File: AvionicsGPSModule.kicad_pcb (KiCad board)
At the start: 4 copper layers, 60 x 56.1 mm, 34 parts, among them P1 MC311D, Q1 AO3400A, U1 RP2040, U2 AP2112K-3.3, U3 L80-R, U4 W25Q128JVS, X1 ABM8-272-T3

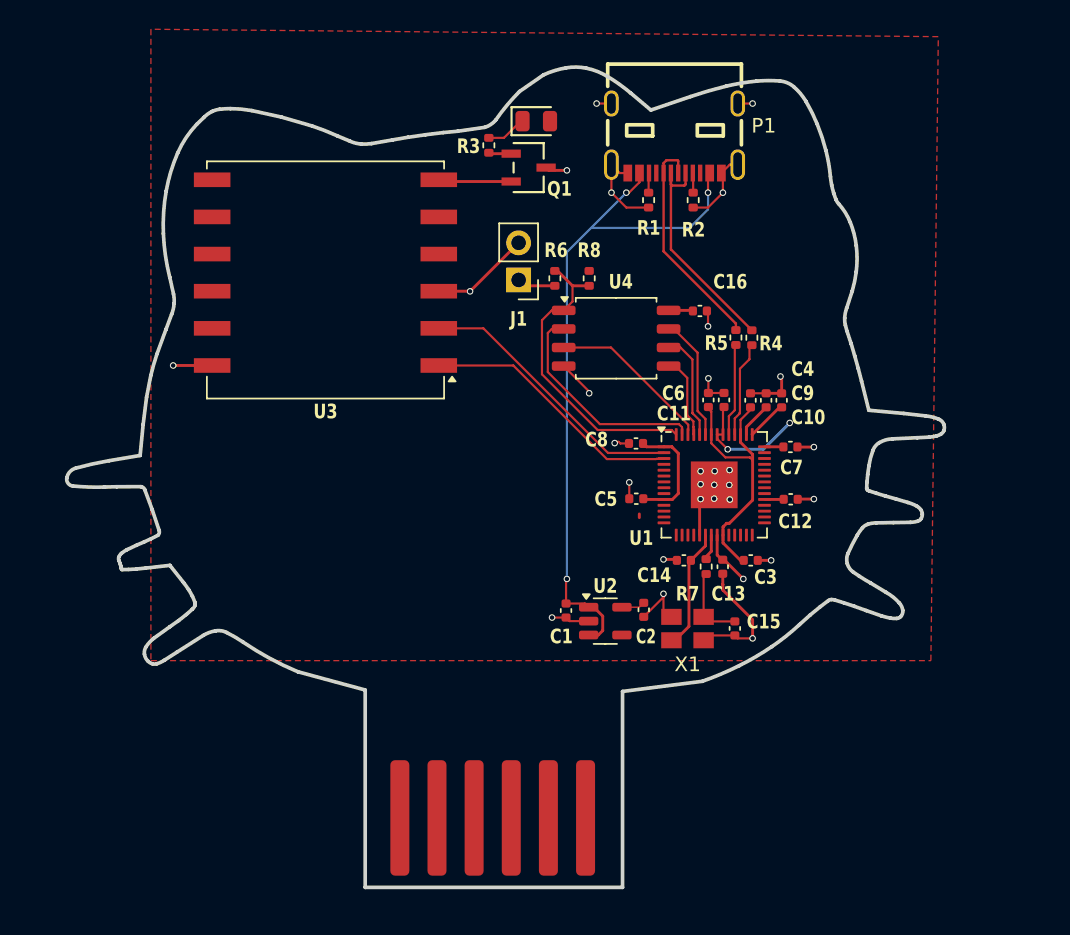
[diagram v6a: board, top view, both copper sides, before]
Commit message: Added mounting holes and LEDs, changed outline
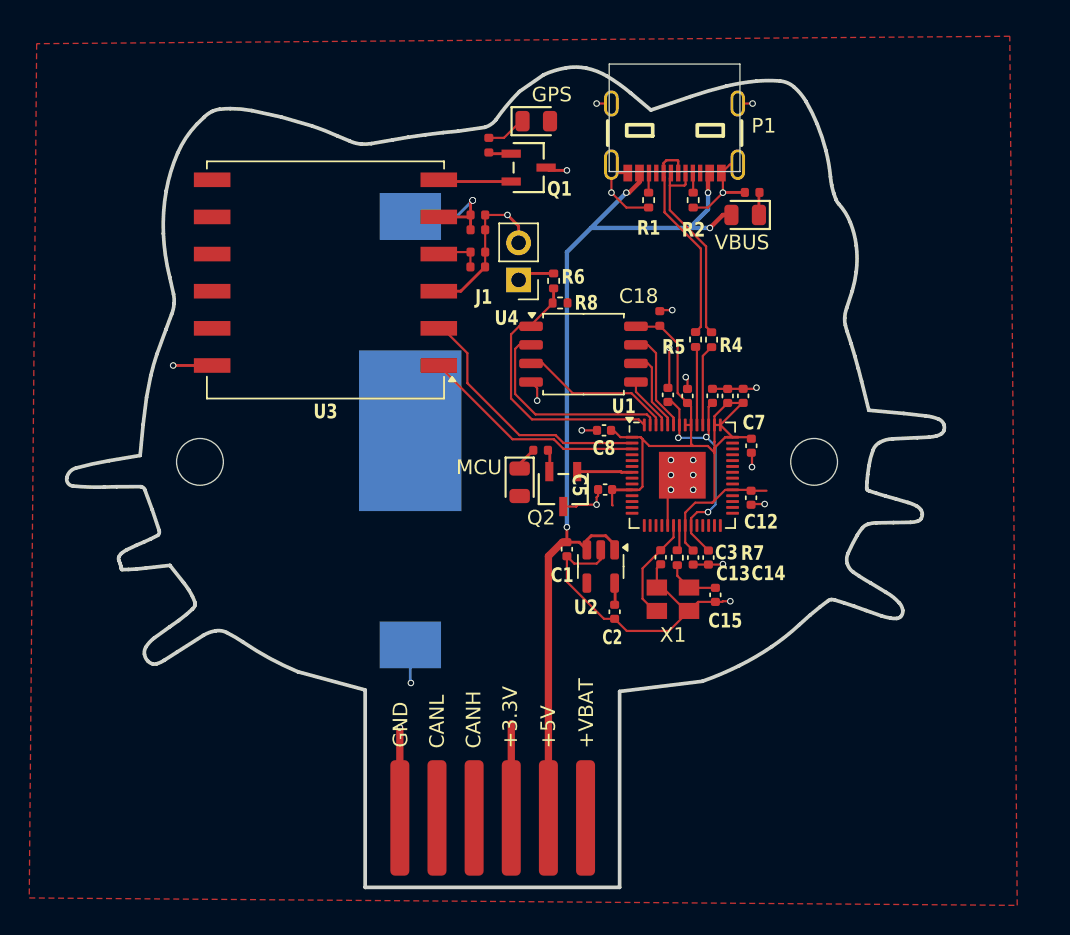
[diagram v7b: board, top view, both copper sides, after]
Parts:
- removed C16: 100n, Capacitor_SMD:C_0402_1005Metric
- removed the REF** at (137.6, 98.2)
- added C17: 10uF, PCM_JLCPCB:C_0402, F.Cu at (135.1, 83.8)
- added C18: 100nF, PCM_JLCPCB:C_0402, F.Cu at (147.6, 87.3)
- added C19: 100nF, PCM_JLCPCB:C_0402, F.Cu at (135.1, 80.3)
- added C20: 4.7uF, PCM_JLCPCB:C_0402, F.Cu at (135.1, 81.3)
- added C21: 100nF, PCM_JLCPCB:C_0402, F.Cu at (135.1, 82.8)
- added D2: Green, PCM_JLCPCB:D_0805, F.Cu at (153.4, 80.3)
- added D5: Red, PCM_JLCPCB:D_0805, F.Cu at (138.0, 98.5)
- added Q2: AO3400A, AO3400A:SOT-23-3L_AOS, F.Cu at (141.0, 99.0)
- added R11: 51Ω, PCM_JLCPCB:R_0402, F.Cu at (135.9, 75.5)
- added R12: 51Ω, PCM_JLCPCB:R_0402, F.Cu at (139.4, 96.4)
- added REF**: HELLO-KITTY-OUTLINE, HelloKittyOutline:HELLO-KITTY-OUTLINE, F.Cu at (137.6, 98.2)
- added REF**: BAT_BU2032SM-FH-G, BU2032SM_FH_GTR:BAT_BU2032SM-FH-G, B.Cu at (130.5, 95.0)
- R3: value 200 -> 150Ω; footprint Resistor_SMD:R_0402_1005Metric -> PCM_JLCPCB:R_0402
- moved R3 18.3 mm to (153.9, 78.7), turned to 0 degrees
- moved C1 4.19 mm to (141.2, 103.1)
- moved U2 3.75 mm to (143.5, 104.3), turned to -90 degrees
- moved C3 2.90 mm to (150.9, 103.7), turned to -90 degrees
- moved C6 2.79 mm to (148.1, 92.6)
- moved R4 2.76 mm to (151.1, 88.8)
- moved R5 2.76 mm to (150.0, 88.8)
- moved C12 2.71 mm to (153.8, 99.6), turned to -90 degrees
- moved C7 2.67 mm to (153.8, 96.0), turned to -90 degrees
- moved C15 2.65 mm to (151.4, 106.2)
- moved C9 2.65 mm to (153.3, 92.6)
- moved C10 2.65 mm to (152.2, 92.6)
- moved C4 2.62 mm to (151.2, 92.6)
- moved R8 2.61 mm to (140.8, 86.3), turned to 180 degrees
- moved C11 2.51 mm to (149.5, 92.6)
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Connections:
- R3 pad 1: Net-(D1-Pad1) -> GND
- R3 pad 2: Net-(Q1-D) -> Net-(D2-Pad1)
- U1 pad 7: unconnected-(U1-GPIO5-Pad7) -> Net-(Q2-D)
- U3 pad 4: +3.3V -> Net-(U3-VCC)
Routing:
- net +3.3V: track 31.9 -> 57.9 mm, vias 3 -> 0
- net GND: track 59.4 -> 83.6 mm, vias 29 -> 26
- net +5V: track 47.6 -> 66.1 mm, vias 3 -> 4
- net +BATT: track 0.00 -> 9.02 mm, vias 0 -> 2
- net Net-(Q2-D): track 0.00 -> 3.77 mm
- net Net-(U3-VCC): track 0.00 -> 3.25 mm
- net /RX: track 18.1 -> 15.6 mm
- net /DN: track 15.7 -> 13.4 mm
- net /QSPI_SDO: track 5.67 -> 3.67 mm
- net /QSPI_SS: track 21.0 -> 19.1 mm
- net +1V1: track 18.7 -> 16.8 mm, vias 0 -> 3
- net Net-(D5-Pad1): track 0.00 -> 1.82 mm
- net /QSPI_SCLK: track 7.31 -> 5.58 mm
- net Net-(C15-Pad1): track 5.25 -> 3.68 mm
- net Net-(D2-Pad1): track 0.00 -> 1.56 mm
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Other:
- outline, holes or cut-outs redrawn
- board text added: "GPS"
- board text added: "MCU"
- board text added: "VBUS"

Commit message: Added Marketing, fulfilled DRC, finalized board
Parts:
- added G***: LOGO, logo:LOGO, F.Cu at (122.9, 99.1)
- C1, C10, C11, C12, C13, C14, C15, C2, C3, C4, C5, C6, C7, C8, C9: footprint Capacitor_SMD:C_0402_1005Metric -> Library:C_0402_1005Metric
- C17, C18, C19, C20, C21: footprint PCM_JLCPCB:C_0402 -> Library:C_0402_1005Metric
- P1: footprint MC-311D:USB-C-SMD_MC-311D -> Connector_USB:USB_C_Receptacle_GCT_USB4105-xx-A_16P_TopMnt_Horizontal
- moved C1 2.41 mm to (143.1, 101.7), turned to 0 degrees
- moved P1 1.48 mm to (148.6, 73.5)
- moved C6 0.48 mm to (148.1, 92.1)
- moved D5 0.43 mm to (137.9, 99.0)
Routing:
- net +3.3V: track 57.9 -> 88.0 mm, vias 0 -> 5
- net GND: track 83.6 -> 75.5 mm, vias 26 -> 29
- net +5V: track 66.1 -> 68.2 mm
- net /DN: track 13.4 -> 14.7 mm
- net +1V1: track 16.8 -> 17.4 mm
- net +BATT: vias 2 -> 1
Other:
- board text added: "Designed by: Evan Bhogal"
- board text added: "Lin gan goolie goolie goolie wata, Lin gan goo, lin gan goo."
- board text added: "MARS GPS Board"
